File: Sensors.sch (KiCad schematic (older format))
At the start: 39 parts, among them CN3 CONN_HEADER_SMD_4POS_2MM, CN4 CONN_HEADER_SMD_4POS_2MM, U1 LPS25HB, U10 MPXV4006GP, U11 MPXV4006DP, U12 TLV2333IDR, U17 MPXV4006GP

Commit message: Removed attenuation from analogue sensor signals. Removed old ADC U13. Renamed sensor signal names on ADC sheet
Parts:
- removed R28, R38, R39: 100K_0603_Chip_Resistor,_1%,_0.1W, Resistor_SMD:R_0603_1608Metric, symbol OpenVent:100K_0603_Chip_Resistor,_1%,_0.1W
- removed R33, R42, R43: 200k_0603_Chip_Resistor,_0.1%,_0.1W, Resistor_SMD:R_0603_1608Metric, symbol OpenVent:200k_0603_Chip_Resistor,_0.1%,_0.1W
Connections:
- wire segments 130 -> 121
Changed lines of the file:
@@
 	1    0    0    -1
 $EndComp
-Text GLabel 4450 4650 2    60   Output ~ 0
+Text GLabel 4050 4650 2    60   Output ~ 0
 PRESSURE-SENSOR-PATIENT
-Text GLabel 4450 3350 2    60   Output ~ 0
+Text GLabel 4050 3350 2    60   Output ~ 0
 FLOW-SENSOR
 $Comp
@@
 Gain: 50
 $Comp
-L OpenVent:GND #GND_033
-U 1 1 5F8DD0B7
-P 4250 3900
-F 0 "#GND_033" H 4250 3900 20  0001 C CNN
-F 1 "GND" H 4250 3830 50  0001 C CNN
-F 2 "" H 4250 3900 70  0000 C CNN
-F 3 "" H 4250 3900 70  0000 C CNN
-	1    4250 3900
-	1    0    0    -1
-$EndComp
-$Comp
-L OpenVent:GND #GND_034
-U 1 1 5F8DD0B6
-P 4250 5200
-F 0 "#GND_034" H 4250 5200 20  0001 C CNN
-F 1 "GND" H 4250 5130 50  0001 C CNN
-F 2 "" H 4250 5200 70  0000 C CNN
-F 3 "" H 4250 5200 70  0000 C CNN
-	1    4250 5200
-	1    0    0    -1
-$EndComp
-$Comp
 L OpenVent:GND #GND_031
 U 1 1 5F8DD0B5
@@
 	10250 2475 9950 2475
 Wire Wire Line
-	4250 4650 4250 4800
-Wire Wire Line
-	4250 3350 4250 3500
-Wire Wire Line
 	8050 3425 8050 3475
 Wire Wire Line
@@
 	2750 3650 2750 3750
 Wire Wire Line
-	3500 3350 3700 3350
-Wire Wire Line
 	3350 4350 3350 4450
-Wire Wire Line
-	4250 4650 4450 4650
-Wire Wire Line
-	4100 4650 4250 4650
-Wire Wire Line
-	4250 3350 4450 3350
-Wire Wire Line
-	4100 3350 4250 3350
 Wire Wire Line
 	2750 3200 2750 3050
@@
 Connection ~ 4500 2150
 Connection ~ 4500 1350
-Connection ~ 4250 4650
-Connection ~ 4250 3350
 Connection ~ 5700 2050
 Connection ~ 5700 1350
@@
 F 6 "50V" H 2850 4250 50  0001 C CNN "Voltage"
 	1    2850 4250
-	0    -1   -1   0
-$EndComp
-$Comp
-L OpenVent:100K_0603_Chip_Resistor,_1%,_0.1W R38
-U 1 1 5F8DD0A8
-P 3800 3250
-F 0 "R38" H 3800 3200 50  0000 L BNN
-F 1 "100K_0603_Chip_Resistor,_1%,_0.1W" H 3800 3000 50  0001 C CNN
-F 2 "Resistor_SMD:R_0603_1608Metric" H 3800 2910 50  0001 C CNN
-F 3 "" H 3800 2910 50  0001 C CNN
-F 4 "1%" V 1400 -2550 50  0001 C CNN "Tolerance"
-F 5 "100k" H 3900 3050 50  0000 C CNN "Val"
-F 6 "0.1W" H 3800 3250 50  0001 C CNN "Watt"
-	1    3800 3250
-	1    0    0    -1
-$EndComp
-$Comp
-L OpenVent:100K_0603_Chip_Resistor,_1%,_0.1W R39
-U 1 1 5F8DD0A6
-P 3800 4550
-F 0 "R39" H 3800 4500 50  0000 L BNN
-F 1 "100K_0603_Chip_Resistor,_1%,_0.1W" H 3800 4300 50  0001 C CNN
-F 2 "Resistor_SMD:R_0603_1608Metric" H 3800 4210 50  0001 C CNN
-F 3 "" H 3800 4210 50  0001 C CNN
-F 4 "1%" V 1400 -2950 50  0001 C CNN "Tolerance"
-F 5 "100k" H 3900 4350 50  0000 C CNN "Val"
-F 6 "0.1W" H 3800 4550 50  0001 C CNN "Watt"
-	1    3800 4550
-	1    0    0    -1
-$EndComp
-$Comp
-L OpenVent:200k_0603_Chip_Resistor,_0.1%,_0.1W R42
-U 1 1 5F8DD0A5
-P 4150 3800
-F 0 "R42" V 4300 3450 50  0000 L BNN
-F 1 "200k_0603_Chip_Resistor,_0.1%,_0.1W" V 4150 3650 50  0001 C CNN
-F 2 "Resistor_SMD:R_0603_1608Metric" H 4050 3660 50  0001 C CNN
-F 3 "" H 4050 3660 50  0001 C CNN
-F 4 "0.1%" V 4100 3500 50  0000 C CNN "Tolerance"
-F 5 "200k" V 4200 3500 50  0000 C CNN "Val"
-F 6 "0.1W" H 4150 3800 50  0001 C CNN "Watt"
-	1    4150 3800
-	0    -1   -1   0
-$EndComp
-$Comp
-L OpenVent:200k_0603_Chip_Resistor,_0.1%,_0.1W R43
-U 1 1 5F8DD0A4
-P 4150 5100
-F 0 "R43" V 4300 4750 50  0000 L BNN
-F 1 "200k_0603_Chip_Resistor,_0.1%,_0.1W" V 4150 4950 50  0001 C CNN
-F 2 "Resistor_SMD:R_0603_1608Metric" H 4050 4960 50  0001 C CNN
-F 3 "" H 4050 4960 50  0001 C CNN
-F 4 "0.1%" V 4100 4800 50  0000 C CNN "Tolerance"
-F 5 "200k" V 4200 4800 50  0000 C CNN "Val"
-F 6 "0.1W" H 4150 5100 50  0001 C CNN "Watt"
-	1    4150 5100
 	0    -1   -1   0
 $EndComp
@@
 $EndComp
 Connection ~ 2950 4650
-Wire Wire Line
-	2950 4650 3700 4650
 $Comp
 L OpenVent:MPXV4006DP U11
@@
 	1    0    0    -1
 $EndComp
-Text GLabel 4450 5950 2    60   Output ~ 0
+Text GLabel 4050 5950 2    60   Output ~ 0
 PRESSURE-SENSOR-VENT
-$Comp
-L OpenVent:GND #GND_046
-U 1 1 5FF44883
-P 4250 6500
-F 0 "#GND_046" H 4250 6500 20  0001 C CNN
-F 1 "GND" H 4250 6430 50  0001 C CNN
-F 2 "" H 4250 6500 70  0000 C CNN
-F 3 "" H 4250 6500 70  0000 C CNN
-	1    4250 6500
-	1    0    0    -1
-$EndComp
 Wire Wire Line
 	1800 6250 2750 6250
@@
 	2950 6250 2950 6350
 Wire Wire Line
-	4250 5950 4250 6100
-Wire Wire Line
 	2550 5650 2550 5350
 Wire Wire Line
@@
 Wire Wire Line
 	3350 5650 3350 5750
-Wire Wire Line
-	4250 5950 4450 5950
-Wire Wire Line
-	4100 5950 4250 5950
 Connection ~ 2750 6350
 Connection ~ 2750 6250
-Connection ~ 4250 5950
 $Comp
 L OpenVent:470pF_0603_Ceramic_Capacitor,_5%,_100V,_C0G C64
@@
 	0    -1   -1   0
 $EndComp
-$Comp
-L OpenVent:100K_0603_Chip_Resistor,_1%,_0.1W R28
-U 1 1 5FF448BA
-P 3800 5850
-F 0 "R28" H 3800 5800 50  0000 L BNN
-F 1 "100K_0603_Chip_Resistor,_1%,_0.1W" H 3800 5600 50  0001 C CNN
-F 2 "Resistor_SMD:R_0603_1608Metric" H 3800 5510 50  0001 C CNN
-F 3 "" H 3800 5510 50  0001 C CNN
-F 4 "1%" V 1400 -1650 50  0001 C CNN "Tolerance"
-F 5 "100k" H 3900 5650 50  0000 C CNN "Val"
-F 6 "0.1W" H 3800 5850 50  0001 C CNN "Watt"
-	1    3800 5850
-	1    0    0    -1
-$EndComp
-$Comp
-L OpenVent:200k_0603_Chip_Resistor,_0.1%,_0.1W R33
-U 1 1 5FF448C3
-P 4150 6400
-F 0 "R33" V 4300 6050 50  0000 L BNN
-F 1 "200k_0603_Chip_Resistor,_0.1%,_0.1W" V 4150 6250 50  0001 C CNN
-F 2 "Resistor_SMD:R_0603_1608Metric" H 4050 6260 50  0001 C CNN
-F 3 "" H 4050 6260 50  0001 C CNN
-F 4 "0.1%" V 4100 6100 50  0000 C CNN "Tolerance"
-F 5 "200k" V 4200 6100 50  0000 C CNN "Val"
-F 6 "0.1W" H 4150 6400 50  0001 C CNN "Watt"
-	1    4150 6400
-	0    -1   -1   0
-$EndComp
 Wire Wire Line
 	2550 5350 2950 5350
@@
 	1800 5950 2950 5950
 Connection ~ 2950 5950
-Wire Wire Line
-	2950 5950 3700 5950
 $Comp
 L OpenVent:MPXV4006GP U17
@@
 Wire Wire Line
 	1350 2050 2000 2050
+Wire Wire Line
+	3500 3350 4050 3350
+Wire Wire Line
+	2950 4650 4050 4650
+Wire Wire Line
+	2950 5950 4050 5950
 $EndSCHEMATC

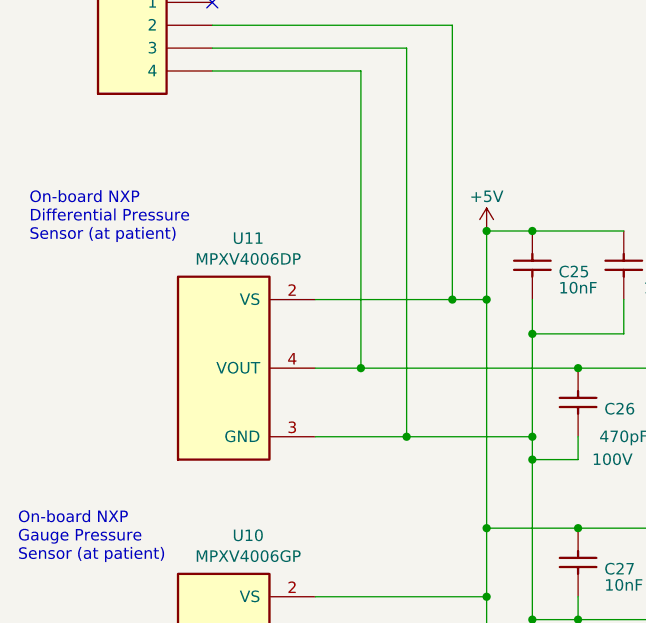
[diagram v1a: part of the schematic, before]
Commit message: Added zero ohm resistors as jumpers to disconnect U11 pins 2 and 4 when Sensirion sensor is used
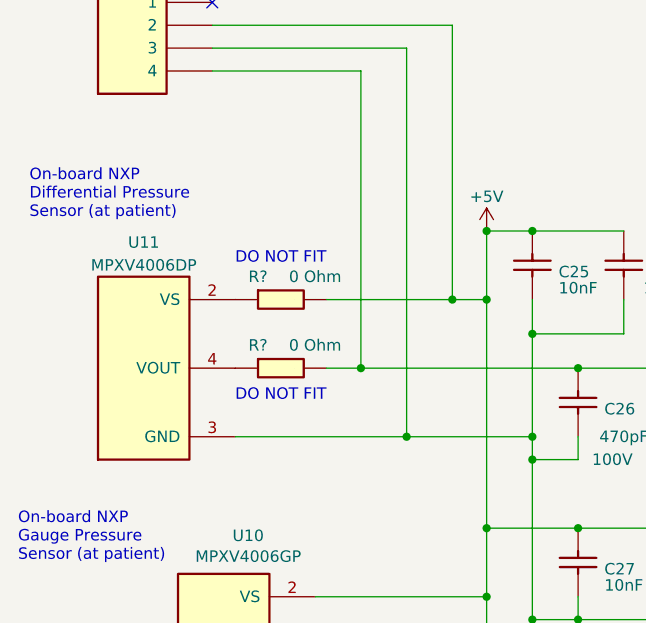
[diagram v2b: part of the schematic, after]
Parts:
- added R? (x2): 0R0_0603_Chip_Resistor,_1%,_0.1W, symbol OpenVent:0R0_0603_Chip_Resistor,_1%,_0.1W
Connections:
- net +5V: now also R?.2; no longer U11.2 (VS)
- net FLOW-SENSOR: now also R?.2; no longer U11.4 (VOUT)
- new net: R?.1, U11.2 (VS)
- new net: R?.1, U11.4 (VOUT)
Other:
- note added: "DO NOT FIT"
- moved on the sheet: U11
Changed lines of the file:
@@
 L OpenVent:MPXV4006DP U11
 U 1 1 5FCDD7C7
-P 1800 3650
-F 0 "U11" H 2093 4517 50  0000 C CNN
-F 1 "MPXV4006DP" H 2093 4426 50  0000 C CNN
-F 2 "OpenVent:NXP-CASE-1351-482C" H 2000 4350 50  0001 C CNN
-F 3 "https://media.digikey.com/pdf/Data%20Sheets/Freescale%20Semi/MPXV4006G.pdf" H 2000 4350 50  0001 C CNN
-F 4 "SENSOR PRESSURE DUAL SMD 8-SOP" H 1800 3650 50  0001 C CNN "Desc"
-F 5 "Pressure Sensor" H 1800 3650 50  0001 C CNN "Detailed"
-F 6 "DigiKey" H 1800 3650 50  0001 C CNN "DistName"
-F 7 "MPXV4006DP-ND" H 1800 3650 50  0001 C CNN "Dist_PN"
-F 8 "NXP USA Inc." H 1800 3650 50  0001 C CNN "Mfr"
-F 9 "MPXV4006DP" H 1800 3650 50  0001 C CNN "Mfr_PN"
-	1    1800 3650
+P 1450 3650
+F 0 "U11" H 1850 4500 50  0000 C CNN
+F 1 "MPXV4006DP" H 1850 4400 50  0000 C CNN
+F 2 "OpenVent:NXP-CASE-1351-482C" H 1650 4350 50  0001 C CNN
+F 3 "https://media.digikey.com/pdf/Data%20Sheets/Freescale%20Semi/MPXV4006G.pdf" H 1650 4350 50  0001 C CNN
+F 4 "SENSOR PRESSURE DUAL SMD 8-SOP" H 1450 3650 50  0001 C CNN "Desc"
+F 5 "Pressure Sensor" H 1450 3650 50  0001 C CNN "Detailed"
+F 6 "DigiKey" H 1450 3650 50  0001 C CNN "DistName"
+F 7 "MPXV4006DP-ND" H 1450 3650 50  0001 C CNN "Dist_PN"
+F 8 "NXP USA Inc." H 1450 3650 50  0001 C CNN "Mfr"
+F 9 "MPXV4006DP" H 1450 3650 50  0001 C CNN "Mfr_PN"
+	1    1450 3650
 	-1   0    0    -1
 $EndComp
@@
 Text Notes 8000 4050 0    50   ~ 0
 On-Board STMicroelectronics Absolute Pressure Sensor
-Text Notes 550  2800 0    50   ~ 0
+Text Notes 550  2700 0    50   ~ 0
 On-board NXP\nDifferential Pressure\nSensor (at patient)
 Text Notes 500  4200 0    50   ~ 0
@@
 Wire Wire Line
 	2400 1850 2400 3050
-Connection ~ 2400 3050
 Wire Wire Line
 	2400 3050 2550 3050
 Wire Wire Line
-	1800 3050 2400 3050
-Wire Wire Line
 	1350 1850 2400 1850
-Wire Wire Line
-	1800 3650 2200 3650
 Wire Wire Line
 	2200 3650 2200 1950
@@
 Wire Wire Line
 	2200 1950 1350 1950
+Wire Wire Line
+	2000 3350 2950 3350
+Wire Wire Line
+	1350 2050 2000 2050
+Wire Wire Line
+	3500 3350 4050 3350
+Wire Wire Line
+	2950 4650 4050 4650
+Wire Wire Line
+	2950 5950 4050 5950
+$Comp
+L OpenVent:0R0_0603_Chip_Resistor,_1%,_0.1W R?
+U 1 1 606B0541
+P 1550 2950
+F 0 "R?" H 1550 2950 50  0000 C CNN
+F 1 "0R0_0603_Chip_Resistor,_1%,_0.1W" H 1550 2950 50  0001 C CNN
+F 2 "" H 1550 2950 50  0001 C CNN
+F 3 "" H 1550 2950 50  0001 C CNN
+F 4 "0 Ohm" H 1800 2950 50  0000 C CNN "Val"
+F 5 "1%" H 1550 2950 50  0001 C CNN "Tolerance"
+F 6 "0.1W" H 1550 2950 50  0001 C CNN "Watt"
+	1    1550 2950
+	1    0    0    -1
+$EndComp
+$Comp
+L OpenVent:0R0_0603_Chip_Resistor,_1%,_0.1W R?
+U 1 1 606B0AE4
+P 1550 3250
+F 0 "R?" H 1550 3250 50  0000 C CNN
+F 1 "0R0_0603_Chip_Resistor,_1%,_0.1W" H 1550 3250 50  0001 C CNN
+F 2 "" H 1550 3250 50  0001 C CNN
+F 3 "" H 1550 3250 50  0001 C CNN
+F 4 "0 Ohm" H 1800 3250 50  0000 C CNN "Val"
+F 5 "1%" H 1550 3250 50  0001 C CNN "Tolerance"
+F 6 "0.1W" H 1550 3250 50  0001 C CNN "Watt"
+	1    1550 3250
+	1    0    0    -1
+$EndComp
+Wire Wire Line
+	1450 3650 2200 3650
+Wire Wire Line
+	1850 3050 2400 3050
+Connection ~ 2400 3050
+Wire Wire Line
+	1850 3350 2000 3350
 Connection ~ 2000 3350
-Wire Wire Line
-	2000 3350 2950 3350
-Wire Wire Line
-	1800 3350 2000 3350
-Wire Wire Line
-	1350 2050 2000 2050
-Wire Wire Line
-	3500 3350 4050 3350
-Wire Wire Line
-	2950 4650 4050 4650
-Wire Wire Line
-	2950 5950 4050 5950
+Text Notes 1450 3500 0    50   ~ 0
+DO NOT FIT
+Text Notes 1450 2900 0    50   ~ 0
+DO NOT FIT
 $EndSCHEMATC

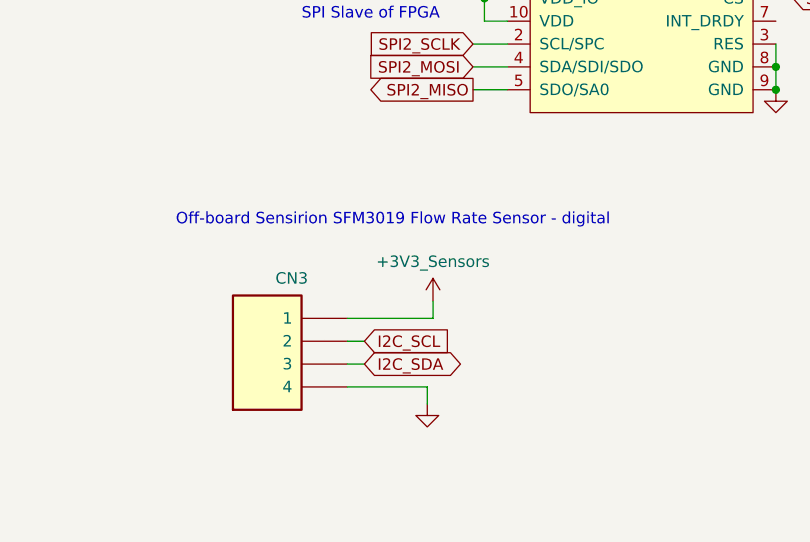
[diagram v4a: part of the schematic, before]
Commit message: Update Sensors.sch
Power for I2C sensor
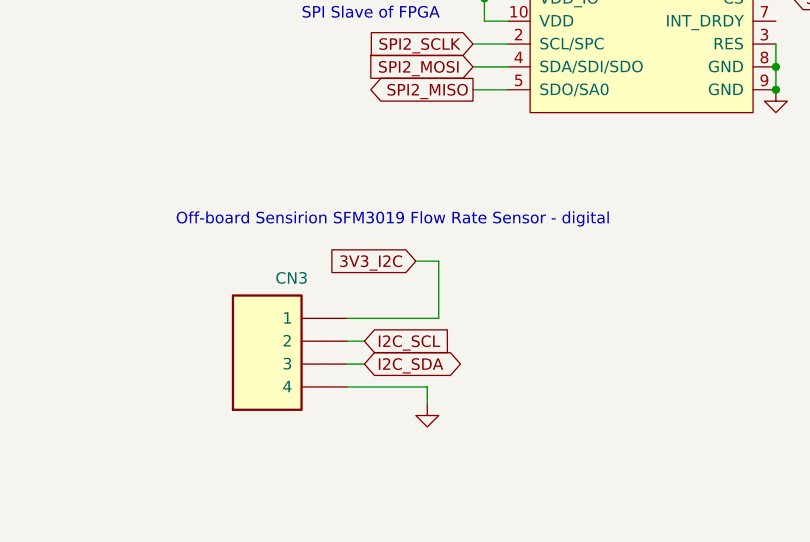
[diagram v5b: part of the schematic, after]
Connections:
- net +3.3V renamed 3V3_I2C
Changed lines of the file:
@@
 Connection ~ 2750 5750
-$Comp
-L OpenVent:+3V3_Sensors #PWR03
-U 1 1 6027FA4F
-P 8025 5675
-F 0 "#PWR03" H 8025 5525 50  0001 C CNN
-F 1 "+3V3_Sensors" H 8025 5848 50  0000 C CNN
-F 2 "" H 8025 5675 50  0001 C CNN
-F 3 "" H 8025 5675 50  0001 C CNN
-	1    8025 5675
-	1    0    0    -1
-$EndComp
 $Comp
 L OpenVent:GND #PWR01
@@
 Wire Wire Line
 	8000 6050 8000 6125
-Wire Wire Line
-	7650 5750 8025 5750
-Wire Wire Line
-	8025 5750 8025 5675
 Text GLabel 7725 5850 2    50   Input ~ 0
 I2C_SCL
@@
 Text Notes 1450 2900 0    50   ~ 0
 DO NOT FIT
+Text GLabel 7950 5500 0    50   Input ~ 0
+3V3_I2C
+Wire Wire Line
+	7650 5750 8050 5750
+Wire Wire Line
+	8050 5750 8050 5500
+Wire Wire Line
+	8050 5500 7950 5500
 $EndSCHEMATC

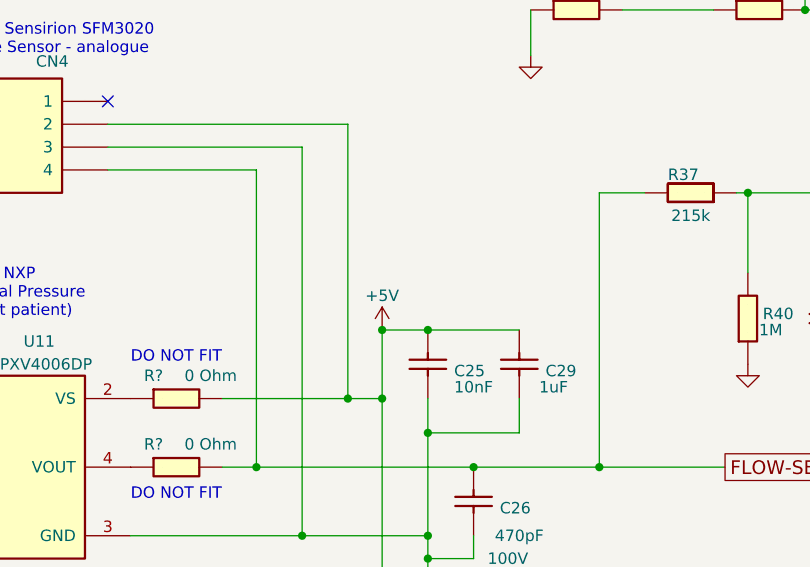
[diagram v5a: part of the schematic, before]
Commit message: Changed sensors to +5V_sensors rail
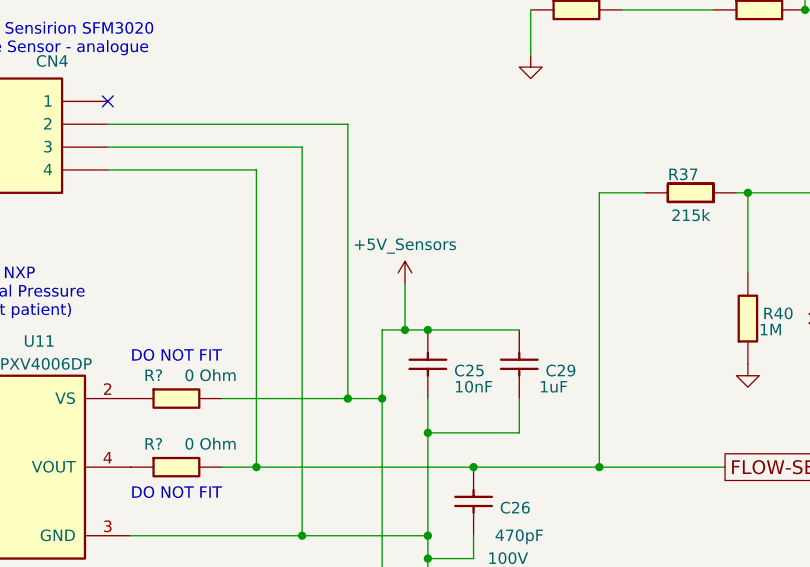
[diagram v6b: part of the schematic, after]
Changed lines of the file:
@@
 $Descr A4 11693 8268
 encoding utf-8
-Sheet 6 9
+Sheet 6 10
 Title "OpenVent Control Board"
 Date "2020-10-20"
@@
 Comment4 ""
 $EndDescr
-$Comp
-L OpenVent:+5V #5V_07
-U 1 1 5F8DD0C0
-P 2550 2750
-F 0 "#5V_07" H 2550 2750 20  0001 C CNN
-F 1 "+5V" H 2550 2900 50  0000 C CNN
-F 2 "" H 2550 2750 70  0000 C CNN
-F 3 "" H 2550 2750 70  0000 C CNN
-	1    2550 2750
-	1    0    0    -1
-$EndComp
 Text GLabel 4050 4650 2    60   Output ~ 0
 PRESSURE-SENSOR-PATIENT
@@
 Wire Wire Line
 	5800 2050 5700 2050
-Connection ~ 2550 2750
 Connection ~ 2750 4950
 Connection ~ 2750 3650
@@
 	2550 4050 2950 4050
 Wire Wire Line
-	2550 2750 2750 2750
+	2550 2750 2650 2750
 Wire Wire Line
 	7650 1475 8050 1475
@@
 Wire Wire Line
 	8050 5500 7950 5500
+$Comp
+L OpenVent:+5V_Sensors #PWR?
+U 1 1 60B19CF0
+P 2650 2550
+F 0 "#PWR?" H 2650 2400 50  0001 C CNN
+F 1 "+5V_Sensors" H 2650 2723 50  0000 C CNN
+F 2 "" H 2650 2550 50  0001 C CNN
+F 3 "" H 2650 2550 50  0001 C CNN
+	1    2650 2550
+	1    0    0    -1
+$EndComp
+Wire Wire Line
+	2650 2750 2650 2550
+Connection ~ 2650 2750
+Wire Wire Line
+	2650 2750 2750 2750
 $EndSCHEMATC

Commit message: Rick's changes - April 19
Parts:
- removed C25, C27: 10nF_0603_Ceramic_Capacitor,_10%,_50V,_X7R-, Capacitor_SMD:C_0603_1608Metric, symbol OpenVent:10nF_0603_Ceramic_Capacitor,_10%,_50V,_X7R-
- removed C26, C28: 470pF_0603_Ceramic_Capacitor,_5%,_100V,_C0G, Capacitor_SMD:C_0603_1608Metric, symbol OpenVent:470pF_0603_Ceramic_Capacitor,_5%,_100V,_C0G
- removed C29, C30: 1uF_0603_Ceramic_Capacitor,_10%,_50V,_X5R, Capacitor_SMD:C_0603_1608Metric, symbol OpenVent:1uF_0603_Ceramic_Capacitor,_10%,_50V,_X5R
- added C? (x2): 470pF_0603_Ceramic_Capacitor,_5%,_100V,_C0G, Capacitor_SMD:C_0603_1608Metric, symbol OpenVent:470pF_0603_Ceramic_Capacitor,_5%,_100V,_C0G
- added C? (x2): 1uF_0603_Ceramic_Capacitor,_10%,_50V,_X5R, Capacitor_SMD:C_0603_1608Metric, symbol OpenVent:1uF_0603_Ceramic_Capacitor,_10%,_50V,_X5R
- added C? (x2): 10nF_0603_Ceramic_Capacitor,_10%,_50V,_X7R-, Capacitor_SMD:C_0603_1608Metric, symbol OpenVent:10nF_0603_Ceramic_Capacitor,_10%,_50V,_X7R-
- added C? (x9): C_1206_47nF_16V_2%_PPS_film, Capacitor_SMD:C_1206_3216Metric, symbol OpenVent:C_1206_47nF_16V_2%_PPS_film
- added C?: 100nF_0603_Ceramic_Capacitor,_10%,_X7R,_25V, Capacitor_SMD:C_0603_1608Metric, symbol OpenVent:100nF_0603_Ceramic_Capacitor,_10%,_X7R,_25V
- added FB?: Chip_Ferrite,_600R,_0603,_750mA, symbol OpenVent:Chip_Ferrite,_600R,_0603,_750mA
- added R?: 100K_0603_Chip_Resistor,_1%,_0.1W, symbol OpenVent:100K_0603_Chip_Resistor,_1%,_0.1W
- added R? (x14): R_0603_47K_0.1%_0.1W_Film, Resistor_SMD:R_0603_1608Metric_Pad0.98x0.95mm_HandSolder, symbol OpenVent:R_0603_47K_0.1%_0.1W_Film
- added TP? (x8): Test_Point_PTH, symbol OpenVent:Test_Point_PTH
- added U?: 74ACT244PW, symbol OpenVent:74ACT244PW
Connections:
- net OXYGEN-SENSOR is gone; now on net O2_SENS: C34.2, R48.2
- net +5V: now also U12.8 (V+), C?.2, C?.2, C?.2, C?.2, FB?.1
- net 3V3_I2C: now also C?.2
- net GND: now also U12.4 (V-), C?.1, C?.1, C?.1, C?.1, C?.1, C?.1, C?.1, C?.2, C?.2, C?.2, C?.2, C?.2, C?.2, C?.2, C?.2, C?.2, U?.1 (1OE), U?.10 (GND), U?.19 (2OE)
- net O2_SENS: now reaches U12.1 (OUTA)
- net O2_SENS: now also R?.1
- net at U12.2 (INA-): now also C34.1, R46.2, R48.1
- net at U12.3 (INA+): now also C33.1, R45.2, R47.1
- net FLOW-SENSOR renamed FLOW_SENS_DRCT
- net FLOW_SENS_DRCT: now also C?.2, R?.1
- net FLOW-SENSOR-GAIN renamed FLOW_SENS_GAIN
- net FLOW_SENS_GAIN: now also R?.1
- net PRESSURE-SENSOR-PATIENT renamed PRES_SENS_PAT
- net PRES_SENS_PAT: now also C?.2, R?.1
- net PRESSURE-SENSOR-VENT renamed PRES_SENS_VENT
- net PRES_SENS_VENT: now also R?.1
- net SPI2_PRESSURE_CS renamed SPI2_PRES_CS
- new net: R?.2, U?.18 (1Y0)
- new net: C?.1, FB?.2, U?.20 (VCC)
- new net: R?.2, U?.9 (2Y3)
- new net: R?.2, U?.12 (1Y3)
- new net: R?.2, U?.14 (1Y2)
- new net: R?.2, U?.16 (1Y1)
- new net: R?.2, U?.3 (2Y0)
- new net: R?.2, U?.5 (2Y1)
- new net: R?.2, U?.7 (2Y2)
- new net AD_VREF: C?.1, R?.1, TP?.1
- new net DRV_FLOW_SENS_DRCT: U?.8 (1A3)
- new net DRV_FLOW_SENS_GAIN: U?.17 (2A0)
- new net DRV_O2_SENS: U?.15 (2A1)
- new net DRV_PRES_SENS_PAT: U?.6 (1A2)
- new net DRV_PRES_SENS_VENT: U?.4 (1A1)
- new net F_DRV: U?.13 (2A2)
- new net G_DRV: U?.11 (2A3)
- new net SensorOut_F: R?.1
- new net SensorOut_G: R?.1
- new net Vcap_F: C?.1, R?.1, R?.2, TP?.1
- new net Vcap_FLOW_SENS_DRCT: C?.1, R?.1, R?.2, TP?.1
- new net Vcap_FLOW_SENS_GAIN: C?.1, R?.1, R?.2, TP?.1
- new net Vcap_G: C?.1, R?.1, R?.2, TP?.1
- new net Vcap_O2_SENS: C?.1, R?.1, R?.2, TP?.1
- new net Vcap_PRES_SENS_PAT: C?.1, R?.1, R?.2, TP?.1
- new net Vcap_PRES_SENS_VENT: C?.1, R?.1, R?.2, TP?.1
- new net Vref_DRV: U?.2 (1A0)
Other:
- note added: "Differential Pressure Sensor\n(at flow sensor)"
- note added: "FPGA ADC analog circuitry"
- note added: "Gauge Pressure Sensor (at flow sensor)"
- note added: "Gauge Pressure Sensor (at patient)"
- note removed: "On-board NXP\nDifferential Pressure\nSensor (at patient)"
- note removed: "On-board NXP\nGauge Pressure\nSensor (at patient)"
- moved on the sheet: C2, C22, C31, C32, C33, C34, C35, C64, C68, CN3, CN4, R27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
